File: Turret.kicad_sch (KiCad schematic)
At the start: 28 parts

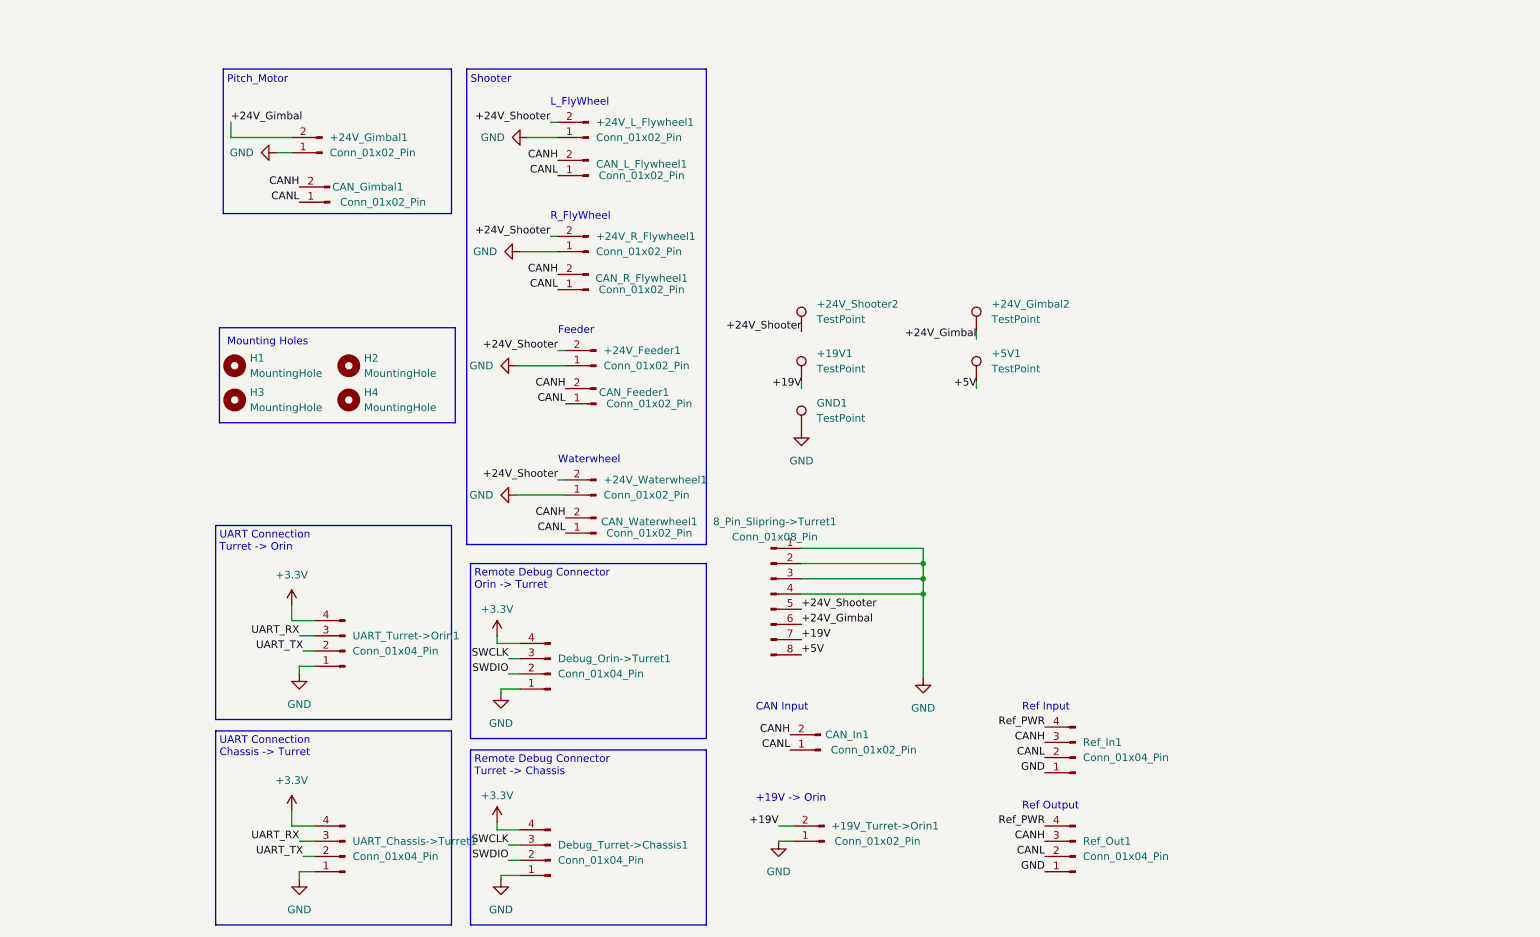
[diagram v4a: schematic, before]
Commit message: New CAN Line, cleaned up schematic, changed pcb
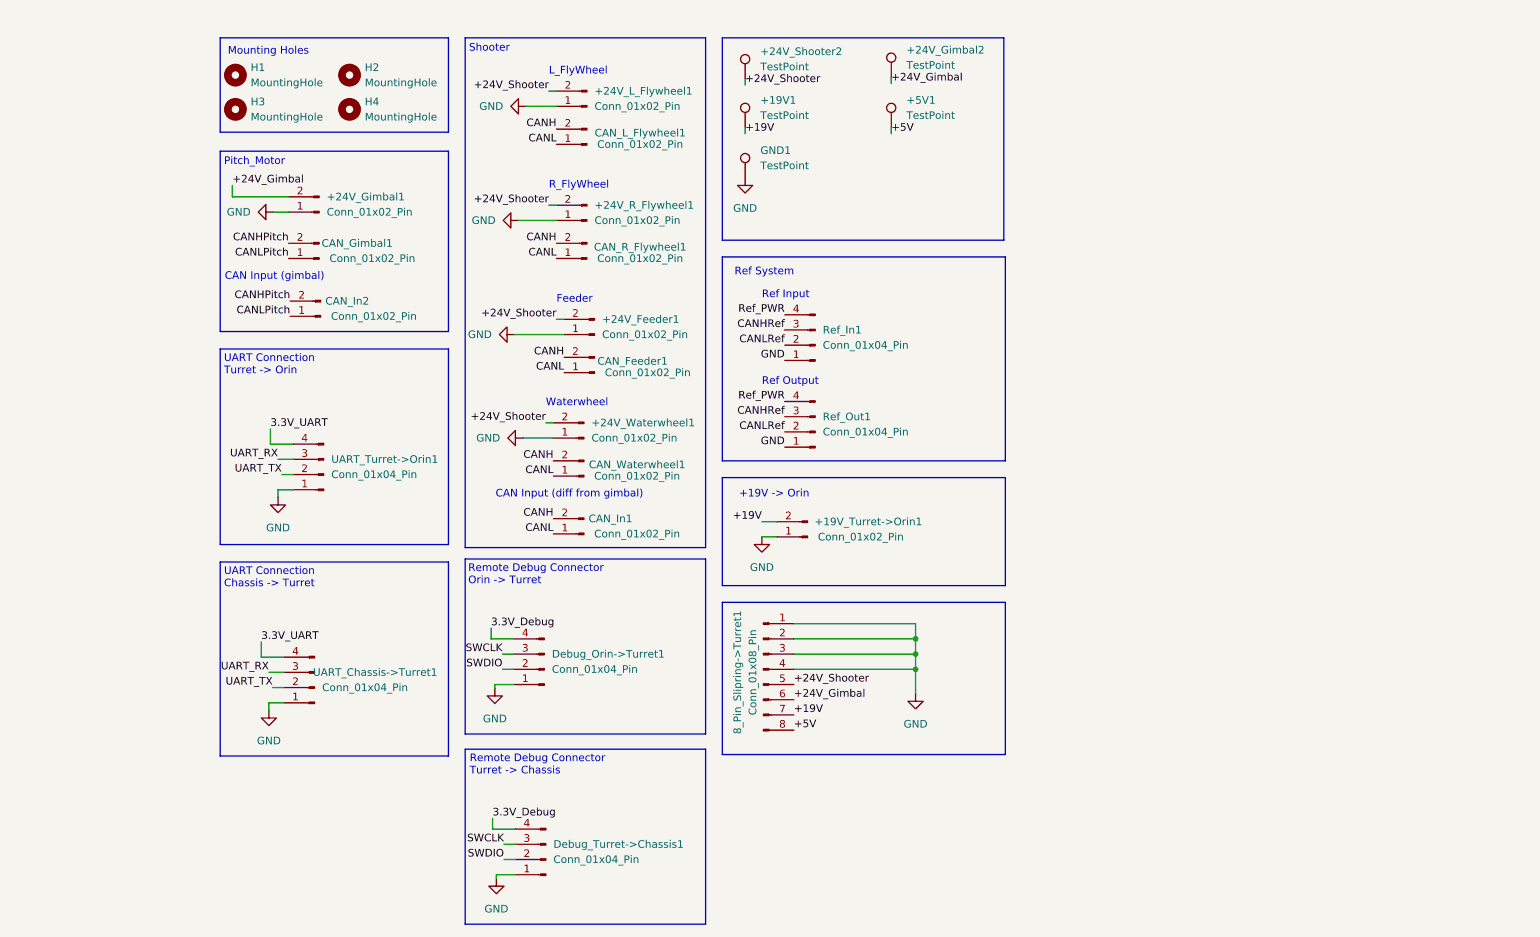
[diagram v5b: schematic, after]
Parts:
- added CAN_In2: Conn_01x02_Pin, Connector_JST:JST_GH_BM02B-GHS-TBT_1x02-1MP_P1.25mm_Vertical, symbol Connector:Conn_01x02_Pin
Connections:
- net CANH: no longer CAN_Gimbal1.2 (Pin_2), Ref_In1.3 (Pin_3), Ref_Out1.3 (Pin_3)
- net CANL: no longer CAN_Gimbal1.1 (Pin_1), Ref_In1.2 (Pin_2), Ref_Out1.2 (Pin_2)
- net +3.3V renamed 3.3V_Debug
- net 3.3V_Debug: no longer UART_Chassis->Turret1.4 (Pin_4), UART_Turret->Orin1.4 (Pin_4)
- new net 3.3V_UART: UART_Chassis->Turret1.4 (Pin_4), UART_Turret->Orin1.4 (Pin_4)
- new net CANHPitch: CAN_Gimbal1.2 (Pin_2), CAN_In2.2 (Pin_2)
- new net CANHRef: Ref_In1.3 (Pin_3), Ref_Out1.3 (Pin_3)
- new net CANLPitch: CAN_Gimbal1.1 (Pin_1), CAN_In2.1 (Pin_1)
- new net CANLRef: Ref_In1.2 (Pin_2), Ref_Out1.2 (Pin_2)
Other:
- note added: "CAN Input (diff from gimbal)"
- note added: "CAN Input (gimbal)"
- note added: "Ref System"
- note removed: "CAN Input"
- moved on the sheet: +19V1, +19V_Turret->Orin1, +24V_Feeder1, +24V_Gimbal1, +24V_Gimbal2, +24V_L_Flywheel1, +24V_R_Flywheel1, +24V_Shooter2, +24V_Waterwheel1, +5V1, 8_Pin_Slipring->Turret1, CAN_Feeder1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

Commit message: Changed symbol fields
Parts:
- +19V1, +24V_Gimbal2, +24V_Shooter2, +5V1, GND1: Mouser Part Number (none) -> Testpoint
- +19V_Turret->Orin1, +24V_Feeder1, +24V_Gimbal1, +24V_L_Flywheel1, +24V_R_Flywheel1, +24V_Waterwheel1: Mouser Part Number (none) -> XT30
- 8_Pin_Slipring->Turret1: Mouser Part Number (none) -> 538-172298-1108
- CAN_Feeder1, CAN_Gimbal1, CAN_In1, CAN_In2, CAN_L_Flywheel1, CAN_R_Flywheel1, CAN_Waterwheel1: Mouser Part Number (none) -> JST 2 Pin
- Debug_Orin->Turret1, Debug_Turret->Chassis1, Ref_In1, Ref_Out1, UART_Chassis->Turret1, UART_Turret->Orin1: Mouser Part Number (none) -> JST 4 Pin
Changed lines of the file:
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@@
+      (effects (font (size 1.27 1.27)) hide)
+    )
+    (property "Mouser Part Number" "JST 2 Pin" (at 83.058 104.902 0)
       (effects (font (size 1.27 1.27)) hide)
     )
@@
       (effects (font (size 1.27 1.27)) hide)
     )
+    (property "Mouser Part Number" "Testpoint" (at 109.982 45.466 0)
+      (effects (font (size 1.27 1.27)) hide)
+    )
     (pin "1")
     (instances
@@
       (effects (font (size 1.27 1.27)) hide)
     )
+    (property "Mouser Part Number" "" (at 24.892 34.036 0)
+      (effects (font (size 1.27 1.27)) hide)
+    )
     (instances
       (project "Turret"
@@
     )
     (property "Datasheet" "~" (at 139.446 28.702 0)
+      (effects (font (size 1.27 1.27)) hide)
+    )
+    (property "Mouser Part Number" "Testpoint" (at 134.366 28.702 0)
       (effects (font (size 1.27 1.27)) hide)
     )
@@
       (effects (font (size 1.27 1.27)) hide)
     )
+    (property "Mouser Part Number" "JST 2 Pin" (at 38.862 58.928 0)
+      (effects (font (size 1.27 1.27)) hide)
+    )
     (pin "1")
     (pin "2")
@@
     )
     (property "Datasheet" "~" (at 121.666 73.406 0)
+      (effects (font (size 1.27 1.27)) hide)
+    )
+    (property "Mouser Part Number" "JST 4 Pin" (at 121.666 73.406 0)
       (effects (font (size 1.27 1.27)) hide)
     )
@@
       (effects (font (size 1.27 1.27)) hide)
     )
+    (property "Mouser Part Number" "JST 4 Pin" (at 76.708 159.258 0)
+      (effects (font (size 1.27 1.27)) hide)
+    )
     (pin "1")
     (pin "2")
@@
       (effects (font (size 1.27 1.27)) hide)
     )
+    (property "Mouser Part Number" "XT30" (at 83.566 33.528 0)
+      (effects (font (size 1.27 1.27)) hide)
+    )
     (pin "1")
     (pin "2")
@@
     )
     (property "Datasheet" "~" (at 39.624 94.996 0)
+      (effects (font (size 1.27 1.27)) hide)
+    )
+    (property "Mouser Part Number" "JST 4 Pin" (at 39.624 94.996 0)
       (effects (font (size 1.27 1.27)) hide)
     )
@@
       (effects (font (size 1.27 1.27)) hide)
     )
+    (property "Mouser Part Number" "JST 4 Pin" (at 76.454 127.508 0)
+      (effects (font (size 1.27 1.27)) hide)
+    )
     (pin "1")
     (pin "2")
@@
     )
     (property "Datasheet" "~" (at 121.666 87.884 0)
+      (effects (font (size 1.27 1.27)) hide)
+    )
+    (property "Mouser Part Number" "JST 4 Pin" (at 121.666 87.884 0)
       (effects (font (size 1.27 1.27)) hide)
     )
@@
       (effects (font (size 1.27 1.27)) hide)
     )
+    (property "Mouser Part Number" "XT30" (at 120.396 105.41 0)
+      (effects (font (size 1.27 1.27)) hide)
+    )
     (pin "1")
     (pin "2")
@@
     )
     (property "Datasheet" "~" (at 24.892 28.321 0)
+      (effects (font (size 1.27 1.27)) hide)
+    )
+    (property "Mouser Part Number" "" (at 24.892 28.321 0)
       (effects (font (size 1.27 1.27)) hide)
     )
@@
       (effects (font (size 1.27 1.27)) hide)
     )
+    (property "Mouser Part Number" "JST 2 Pin" (at 39.116 68.58 0)
+      (effects (font (size 1.27 1.27)) hide)
+    )
     (pin "1")
     (pin "2")
@@
       (effects (font (size 1.27 1.27)) hide)
     )
+    (property "Mouser Part Number" "XT30" (at 84.836 71.628 0)
+      (effects (font (size 1.27 1.27)) hide)
+    )
     (pin "1")
     (pin "2")
@@
       (effects (font (size 1.27 1.27)) hide)
     )
+    (property "Mouser Part Number" "Testpoint" (at 109.982 28.956 0)
+      (effects (font (size 1.27 1.27)) hide)
+    )
     (pin "1")
     (instances
@@
       (effects (font (size 1.27 1.27)) hide)
     )
+    (property "Mouser Part Number" "" (at 43.942 34.036 0)
+      (effects (font (size 1.27 1.27)) hide)
+    )
     (instances
       (project "Turret"
@@
       (effects (font (size 1.27 1.27)) hide)
     )
+    (property "Mouser Part Number" "Testpoint" (at 109.982 37.084 0)
+      (effects (font (size 1.27 1.27)) hide)
+    )
     (pin "1")
     (instances
@@
       (effects (font (size 1.27 1.27)) hide)
     )
+    (property "Mouser Part Number" "XT30" (at 38.862 51.181 0)
+      (effects (font (size 1.27 1.27)) hide)
+    )
     (pin "1")
     (pin "2")
@@
     )
     (property "Datasheet" "~" (at 83.058 88.9 0)
+      (effects (font (size 1.27 1.27)) hide)
+    )
+    (property "Mouser Part Number" "XT30" (at 83.058 88.9 0)
       (effects (font (size 1.27 1.27)) hide)
     )
@@
     )
     (property "Datasheet" "~" (at 113.03 127.508 0)
+      (effects (font (size 1.27 1.27)) hide)
+    )
+    (property "Mouser Part Number" "538-172298-1108" (at 113.03 127.508 0)
       (effects (font (size 1.27 1.27)) hide)
     )
@@
       (effects (font (size 1.27 1.27)) hide)
     )
+    (property "Mouser Part Number" "Testpoint" (at 134.366 37.084 0)
+      (effects (font (size 1.27 1.27)) hide)
+    )
     (pin "1")
     (instances
@@
     )
     (property "Datasheet" "~" (at 43.942 28.321 0)
+      (effects (font (size 1.27 1.27)) hide)
+    )
+    (property "Mouser Part Number" "" (at 43.942 28.321 0)
       (effects (font (size 1.27 1.27)) hide)
     )
@@
       (effects (font (size 1.27 1.27)) hide)
     )
+    (property "Mouser Part Number" "JST 4 Pin" (at 38.1 130.556 0)
+      (effects (font (size 1.27 1.27)) hide)
+    )
     (pin "1")
     (pin "2")
@@
       (effects (font (size 1.27 1.27)) hide)
     )
+    (property "Mouser Part Number" "JST 2 Pin" (at 83.058 95.25 0)
+      (effects (font (size 1.27 1.27)) hide)
+    )
     (pin "1")
     (pin "2")
@@
       (effects (font (size 1.27 1.27)) hide)
     )
+    (property "Mouser Part Number" "JST 2 Pin" (at 83.566 58.928 0)
+      (effects (font (size 1.27 1.27)) hide)
+    )
     (pin "1")
     (pin "2")
@@
       (effects (font (size 1.27 1.27)) hide)
     )
+    (property "Mouser Part Number" "JST 2 Pin" (at 84.836 77.978 0)
+      (effects (font (size 1.27 1.27)) hide)
+    )
     (pin "1")
     (pin "2")
@@
       (effects (font (size 1.27 1.27)) hide)
     )
+    (property "Mouser Part Number" "JST 2 Pin" (at 83.566 39.878 0)
+      (effects (font (size 1.27 1.27)) hide)
+    )
     (pin "1")
     (pin "2")
@@
       (effects (font (size 1.27 1.27)) hide)
     )
+    (property "Mouser Part Number" "XT30" (at 83.566 52.578 0)
+      (effects (font (size 1.27 1.27)) hide)
+    )

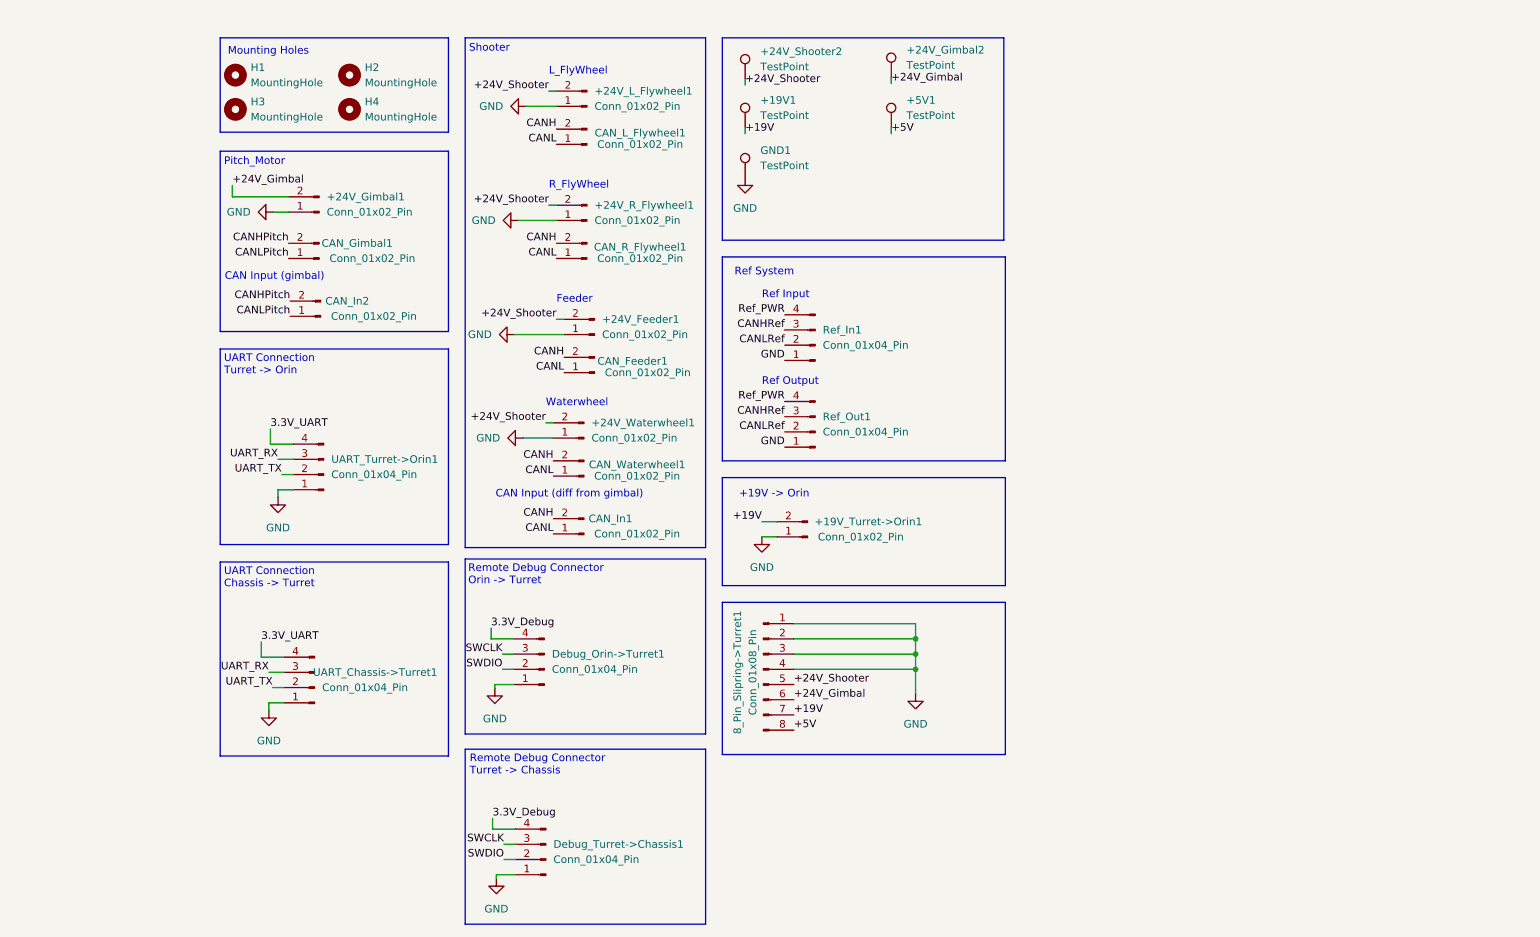
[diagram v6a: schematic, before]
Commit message: added hierarchial labels for input/output characteristics
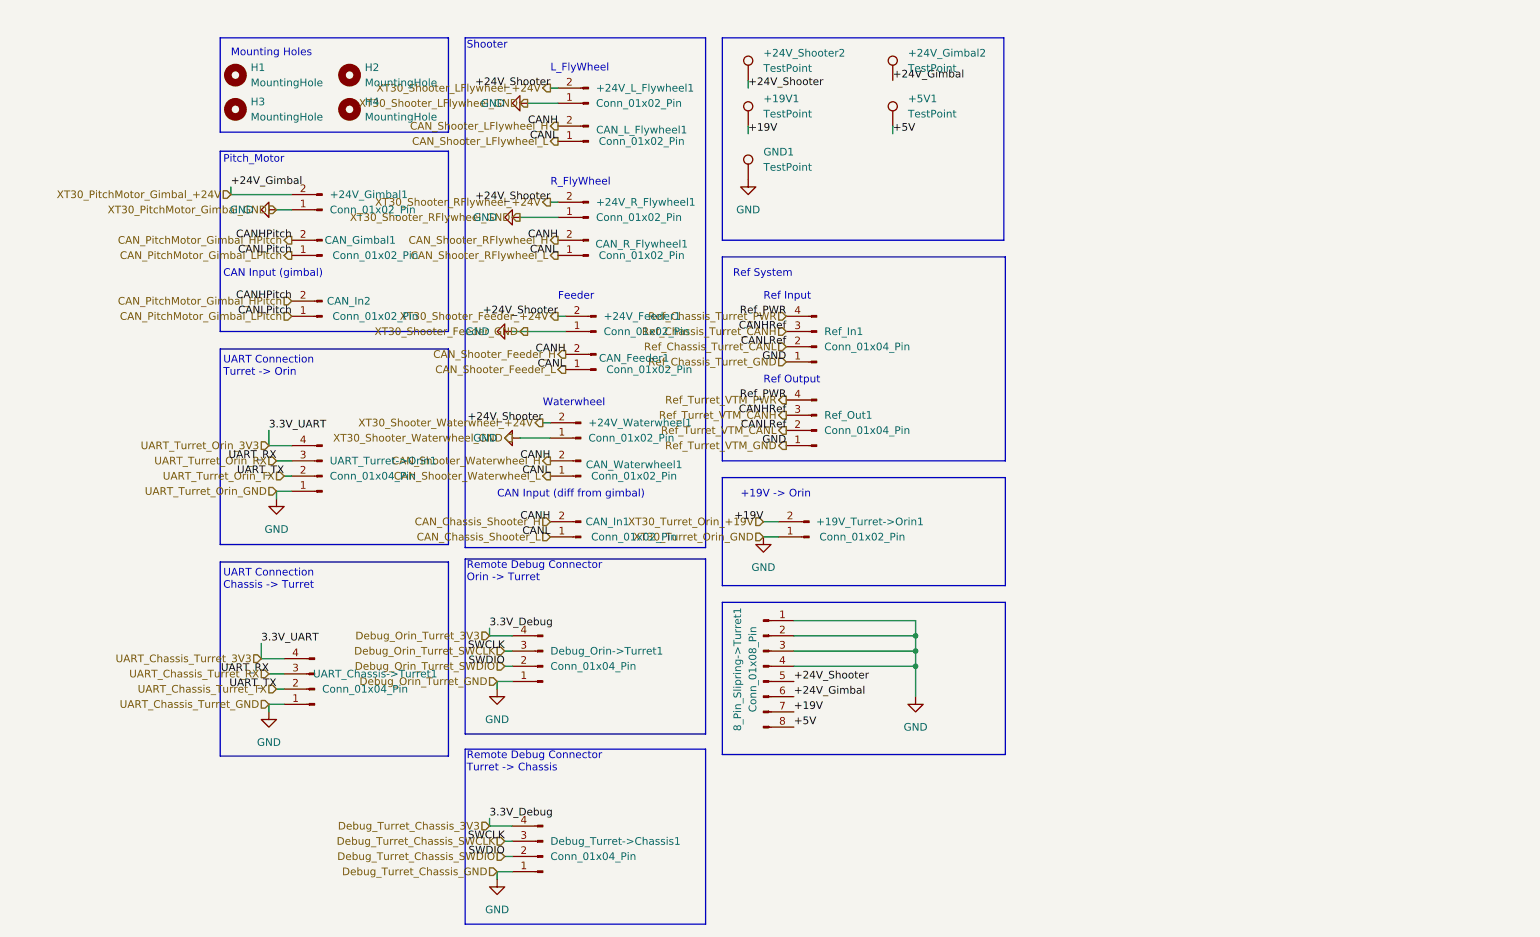
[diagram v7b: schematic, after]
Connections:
- net +19V renamed XT30_Turret_Orin_+19V
- net +24V_Gimbal renamed XT30_PitchMotor_Gimbal_+24V
- net +24V_Shooter renamed XT30_Shooter_Feeder_+24V
- net 3.3V_Debug renamed Debug_Orin_Turret_3V3
- net 3.3V_UART renamed UART_Chassis_Turret_3V3
- net CANH renamed CAN_Chassis_Shooter_H
- net CANHPitch renamed CAN_PitchMotor_Gimbal_HPitch
- net CANHRef renamed Ref_Chassis_Turret_CANH
- net CANL renamed CAN_Chassis_Shooter_L
- net CANLPitch renamed CAN_PitchMotor_Gimbal_LPitch
- net CANLRef renamed Ref_Chassis_Turret_CANL
- net Ref_PWR renamed Ref_Chassis_Turret_PWR
- net SWCLK renamed Debug_Orin_Turret_SWCLK
- net SWDIO renamed Debug_Orin_Turret_SWDIO
- net UART_RX renamed UART_Chassis_Turret_RX
- net UART_TX renamed UART_Chassis_Turret_TX
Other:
- moved on the sheet: +19V1, +24V_Feeder1, +24V_Gimbal1, +24V_Gimbal2, +24V_L_Flywheel1, +24V_R_Flywheel1, +24V_Shooter2, +24V_Waterwheel1, 8_Pin_Slipring->Turret1, CAN_Feeder1, CAN_Gimbal1, CAN_In1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
